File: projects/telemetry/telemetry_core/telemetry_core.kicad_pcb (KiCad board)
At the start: 2 copper layers, 109.3 x 58.3 mm, 60 parts, among them J1 MM_F_RA_20, J2 JST_SM06B-GHS-TB_LF__SN_, J3 CONN_02X03, U1 ATMEGA16M1, U2 TPS560430YF, U3 MCP79511-I_MS, U4 TXB0104PW, U5 LM3480-3.3, U6 MCP2561-E_SN, Y1 Crystal_SMD, Y2 Crystal_32_768kHz

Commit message: feat: begin layout process
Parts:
- moved L1 212.4 mm to (155.2, 43.0), turned to 90 degrees
- moved R11 140.7 mm to (75.1, 120.9)
- moved R5 134.3 mm to (64.9, 89.4)
- moved Y2 132.4 mm to (85.3, 121.3), turned to 90 degrees
- moved U3 130.7 mm to (80.1, 120.5), turned to 180 degrees
- moved R1 127.2 mm to (61.5, 94.4), turned to 90 degrees
- moved C12 126.8 mm to (76.1, 123.1)
- moved C9 123.9 mm to (88.4, 122.3)
- moved C10 121.5 mm to (88.4, 120.3)
- moved D4 121.2 mm to (62.7, 131.6), turned to 180 degrees
- moved D5 120.6 mm to (58.3, 131.6), turned to 180 degrees
- moved D6 120.2 mm to (53.8, 131.6), turned to 180 degrees
- moved R7 118.6 mm to (61.7, 128.9)
- moved TP3 118.5 mm to (53.1, 125.5), turned to 180 degrees
- moved R8 117.5 mm to (57.1, 128.9)
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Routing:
- net GND: track 65.5 -> 105.6 mm, vias 11 -> 27
- net Net-(C2-Pad1): track 0.00 -> 14.8 mm
- net +5V: track 0.00 -> 11.8 mm
- net /12V: track 13.1 -> 19.6 mm
- net +3V3: track 0.00 -> 5.86 mm
- net Net-(C9-Pad1): track 0.00 -> 5.84 mm
- net Net-(C10-Pad1): track 0.00 -> 5.83 mm
- net /P_LED_1: track 0.00 -> 3.06 mm
- net /P_LED_2: track 0.00 -> 2.90 mm
- net /12V_IN: track 0.00 -> 2.66 mm
- net Net-(C7-Pad1): track 0.00 -> 2.61 mm
- net /P_LED_3: track 0.00 -> 2.58 mm
- net /CAN_N: track 0.00 -> 2.49 mm
- net Net-(C5-Pad1): track 0.00 -> 2.41 mm
- net /CAN_P: track 0.00 -> 2.28 mm
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
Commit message: feat: near-complete layout
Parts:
- removed L1: L_100uH, footprints:L_100uH_OEM
- moved C16 150.6 mm to (193.0, 115.3), turned to 270 degrees
- moved U6 140.7 mm to (189.2, 112.3), turned to 90 degrees
- moved R12 139.6 mm to (193.0, 111.8), turned to 90 degrees
- moved C2 138.3 mm to (196.1, 119.6), turned to 90 degrees
- moved R5 137.5 mm to (198.0, 123.8), turned to 270 degrees
- moved C1 134.4 mm to (191.8, 118.2), turned to 180 degrees
- moved R1 134.1 mm to (193.0, 120.4), turned to 0 degrees
- moved U1 127.6 mm to (191.6, 126.9), turned to 270 degrees
- moved C7 120.6 mm to (180.5, 124.2)
- moved Y1 120.6 mm to (182.1, 127.1)
- moved C5 120.6 mm to (184.7, 125.6)
- moved C11 112.9 mm to (184.2, 116.5), turned to 0 degrees
- moved U4 106.4 mm to (182.0, 120.3), turned to 0 degrees
- moved R11 100.2 mm to (175.1, 116.8), turned to 270 degrees
- moved D4 99.8 mm to (162.6, 132.3)
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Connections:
- L101 pad 1: Net-(C103-Pad2) -> Net-(C6-Pad2)
- L101 pad 2: Net-(COUT101-Pad1) -> Net-(COUT1-Pad1)
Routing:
- net +5V: track 11.8 -> 35.5 mm
- net /RXD_RADIO: track 0.00 -> 23.3 mm
- net Net-(COUT101-Pad1): track 17.3 -> 0.00 mm
- net /MOSI: track 0.00 -> 16.5 mm
- net /CAN_RX: track 0.00 -> 15.1 mm
- net /12V: track 19.6 -> 33.7 mm
- net /CSB: track 0.00 -> 9.33 mm
- net /CAN_TX: track 0.00 -> 8.95 mm
- net /SI_ATMEGA: track 0.00 -> 8.49 mm
- net /RTS_RADIO: track 0.00 -> 7.40 mm
- net /CTS_RADIO: track 0.00 -> 7.21 mm
- net Net-(C7-Pad1): track 2.61 -> 9.42 mm
- net Net-(C6-Pad2): track 0.00 -> 5.44 mm
- net Net-(C103-Pad2): track 5.44 -> 0.00 mm
- net /SO_ATMEGA: track 0.00 -> 5.23 mm
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- added copper zone on F.Cu, net +3V3
- added copper zone on F.Cu, net +5V

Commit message: feat: complete v1 layout
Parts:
- moved TP6 128.6 mm to (182.1, 126.0), turned to 270 degrees
- moved TP4 100.7 mm to (169.7, 109.0), turned to 270 degrees
- moved TP5 94.8 mm to (172.6, 102.6), turned to 270 degrees
- moved C14 82.2 mm to (131.7, 114.3)
- moved U5 82.2 mm to (134.6, 114.4)
- moved C13 82.2 mm to (137.8, 114.3)
- moved J3 73.2 mm to (172.2, 146.7), turned to 270 degrees
- moved C15 61.8 mm to (176.0, 94.1), turned to 0 degrees
- moved D7 60.0 mm to (166.6, 97.9)
- moved J1 58.4 mm to (159.4, 90.8), turned to 270 degrees
- moved D2 55.6 mm to (180.9, 102.6), turned to 180 degrees
- moved J2 52.1 mm to (156.5, 148.6), turned to 0 degrees
- moved R2 50.9 mm to (177.2, 102.7), turned to 0 degrees
- moved R3 50.3 mm to (181.6, 116.2), turned to 90 degrees
- moved R4 49.8 mm to (181.6, 120.1), turned to 90 degrees
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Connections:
- U1 pad 23: /P_LED_3 -> /P_LED_2
- U1 pad 24: /P_LED_2 -> /P_LED_3
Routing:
- net +5V: track 35.5 -> 137.0 mm, vias 0 -> 2
- net /MISO: track 0.00 -> 46.5 mm, vias 0 -> 2
- net /CAN_P: track 6.29 -> 36.6 mm
- net +3V3: track 5.86 -> 35.1 mm, vias 0 -> 2
- net /P_LED_2: track 2.90 -> 31.4 mm, vias 0 -> 2
- net /P_LED_1: track 3.06 -> 30.6 mm, vias 0 -> 2
- net /CAN_N: track 4.27 -> 31.1 mm
- net /P_LED_3: track 2.58 -> 27.3 mm, vias 0 -> 2
- net /RESET: track 2.14 -> 26.0 mm, vias 0 -> 2
- net /MOSI: track 16.5 -> 37.9 mm, vias 0 -> 2
- net /RXD_RADIO: track 23.3 -> 41.3 mm, vias 0 -> 2
- net GND: track 101.7 -> 115.2 mm, vias 28 -> 35
- net /RTS_RADIO: track 7.40 -> 17.1 mm
- net /CTS_RADIO: track 7.21 -> 15.7 mm
- net /12V: track 33.7 -> 27.2 mm
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- added copper zone on F.Cu, net Net-(C6-Pad2)
- added copper zone on F.Cu, net Net-(COUT1-Pad1)
- removed copper zone on F.Cu, net Net-(C103-Pad2)
- removed copper zone on F.Cu, net Net-(COUT101-Pad1)
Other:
- board size 109.3 x 58.3 mm -> 76.2 x 63.5 mm
- board text added: "Telemetry Core | V1.0 Melissa Kazazić '24 03/06/2022"

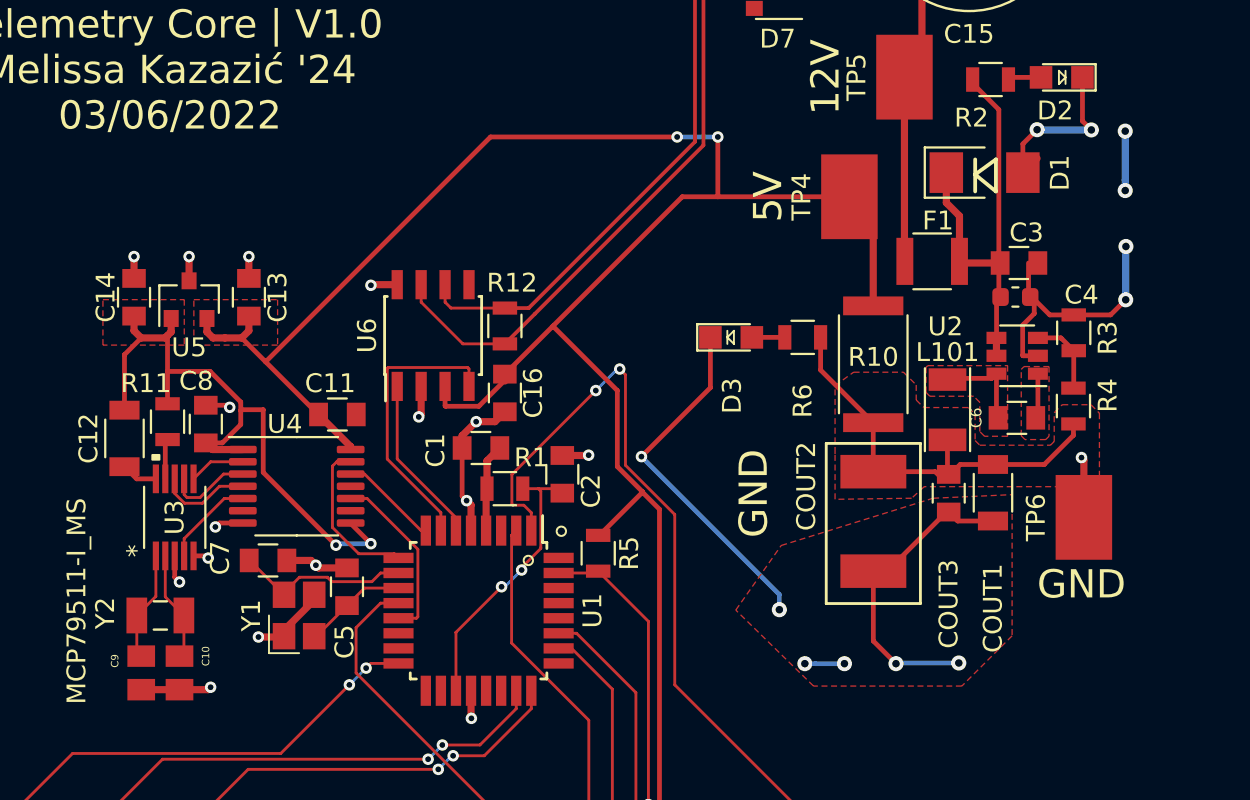
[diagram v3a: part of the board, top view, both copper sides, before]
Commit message: fix: add copper zone
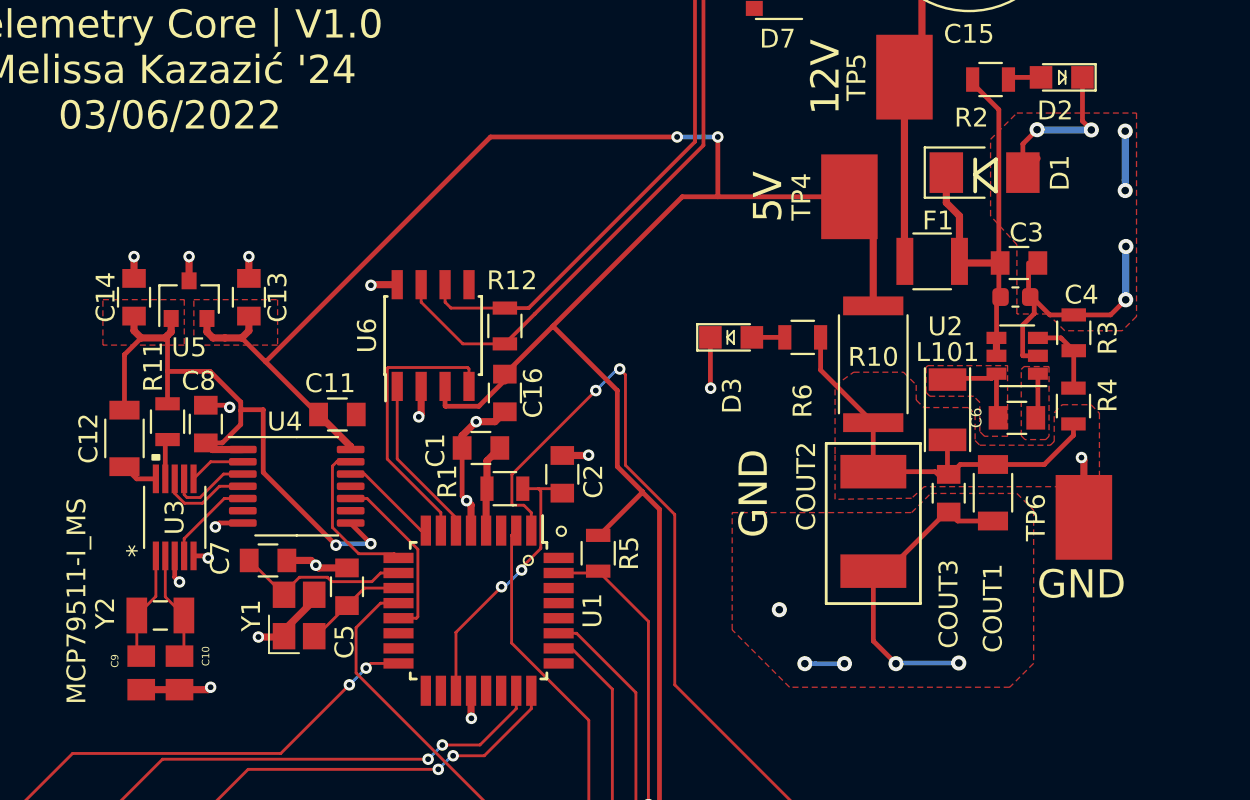
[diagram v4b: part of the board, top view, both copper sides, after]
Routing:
- net GND: track 115.2 -> 98.9 mm
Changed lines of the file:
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@@
     (thickness 1.6)
     (drawings 36)
-    (tracks 467)
+    (tracks 463)
     (zones 0)
     (modules 59)
@@
     (34 B.Paste user)
     (35 F.Paste user)
-    (36 B.SilkS user)
+    (36 B.SilkS user hide)
     (37 F.SilkS user)
     (38 B.Mask user)
@@
     (tags "capacitor 0805")
     (attr smd)
-    (fp_text reference C2 (at -0.889 1.524 90) (layer F.SilkS)
+    (fp_text reference C2 (at -0.381 1.651 90) (layer F.SilkS)
       (effects (font (size 1 1) (thickness 0.15)))
     )
@@
     (tags "capacitor 0805")
     (attr smd)
-    (fp_text reference C8 (at -2.286 0.508) (layer F.SilkS)
+    (fp_text reference C8 (at -2.286 0.381 180) (layer F.SilkS)
       (effects (font (size 1 1) (thickness 0.15)))
     )
@@
       (effects (font (size 1 1) (thickness 0.15)))
     )
-    (fp_line (start 1.75 0.87) (end -1.75 0.87) (layer F.CrtYd) (width 0.05))
-    (fp_line (start 1.75 0.87) (end 1.75 -0.88) (layer F.CrtYd) (width 0.05))
-    (fp_line (start -1.75 -0.88) (end -1.75 0.87) (layer F.CrtYd) (width 0.05))
-    (fp_line (start -1.75 -0.88) (end 1.75 -0.88) (layer F.CrtYd) (width 0.05))
-    (fp_line (start -0.5 0.85) (end 0.5 0.85) (layer F.SilkS) (width 0.12))
-    (fp_line (start 0.5 -0.85) (end -0.5 -0.85) (layer F.SilkS) (width 0.12))
-    (fp_line (start -1 -0.62) (end 1 -0.62) (layer F.Fab) (width 0.1))
-    (fp_line (start 1 -0.62) (end 1 0.62) (layer F.Fab) (width 0.1))
-    (fp_line (start 1 0.62) (end -1 0.62) (layer F.Fab) (width 0.1))
     (fp_line (start -1 0.62) (end -1 -0.62) (layer F.Fab) (width 0.1))
-    (pad 1 smd rect (at -1 0 270) (size 1 1.25) (layers F.Cu F.Paste F.Mask)
-      (net 1 GND))
+    (fp_line (start 1 0.62) (end -1 0.62) (layer F.Fab) (width 0.1))
+    (fp_line (start 1 -0.62) (end 1 0.62) (layer F.Fab) (width 0.1))
+    (fp_line (start -1 -0.62) (end 1 -0.62) (layer F.Fab) (width 0.1))
+    (fp_line (start 0.5 -0.85) (end -0.5 -0.85) (layer F.SilkS) (width 0.12))
+    (fp_line (start -0.5 0.85) (end 0.5 0.85) (layer F.SilkS) (width 0.12))
+    (fp_line (start -1.75 -0.88) (end 1.75 -0.88) (layer F.CrtYd) (width 0.05))
+    (fp_line (start -1.75 -0.88) (end -1.75 0.87) (layer F.CrtYd) (width 0.05))
+    (fp_line (start 1.75 0.87) (end 1.75 -0.88) (layer F.CrtYd) (width 0.05))
+    (fp_line (start 1.75 0.87) (end -1.75 0.87) (layer F.CrtYd) (width 0.05))
     (pad 2 smd rect (at 1 0 270) (size 1 1.25) (layers F.Cu F.Paste F.Mask)
       (net 10 +3V3))
+    (pad 1 smd rect (at -1 0 270) (size 1 1.25) (layers F.Cu F.Paste F.Mask)
+      (net 1 GND))
     (model ${LOCAL_DIR}/OEM_Preferred_Parts/3DModels/C_0805_OEM/C_0805.step
       (at (xyz 0 0 0))
@@
     (tags "resistor 0805")
     (attr smd)
-    (fp_text reference R1 (at 1.397 -1.651 180) (layer F.SilkS)
+    (fp_text reference R1 (at -3.048 -0.381 270) (layer F.SilkS)
       (effects (font (size 1 1) (thickness 0.15)))
     )
@@
     (tags "resistor 0805")
     (attr smd)
-    (fp_text reference R11 (at -2.032 1.143 180) (layer F.SilkS)
+    (fp_text reference R11 (at -2.921 0.762 270) (layer F.SilkS)
       (effects (font (size 1 1) (thickness 0.15)))
     )
@@
     (tags "resistor 0805")
     (attr smd)
-    (fp_text reference R12 (at 2.286 0.381 180) (layer F.SilkS)
+    (fp_text reference R12 (at 2.413 0.381) (layer F.SilkS)
       (effects (font (size 1 1) (thickness 0.15)))
     )
@@
     (tags "TSSOP SO")
     (attr smd)
-    (fp_text reference U4 (at -0.635 -3.302) (layer F.SilkS)
+    (fp_text reference U4 (at -0.635 -3.429) (layer F.SilkS)
       (effects (font (size 1 1) (thickness 0.15)))
     )
@@
   (segment (start 179.63388 106.92892) (end 178.8795 107.6833) (width 0.381) (layer F.Cu) (net 1))
   (via (at 165.95344 130.88366) (size 0.8) (drill 0.4) (layers F.Cu B.Cu) (net 1))
-  (segment (start 165.95344 130.07848) (end 165.95344 130.88366) (width 0.25) (layer B.Cu) (net 1))
-  (segment (start 158.63316 122.7582) (end 158.63316 122.7582) (width 0.25) (layer B.Cu) (net 1))
   (segment (start 178.8795 107.4928) (end 178.8795 107.6833) (width 0.1524) (layer F.Cu) (net 1))
-  (segment (start 162.293 119.09836) (end 158.63316 122.7582) (width 0.254) (layer F.Cu) (net 1))
   (segment (start 162.293 116.429) (end 162.293 119.09836) (width 0.254) (layer F.Cu) (net 1))
   (segment (start 170.942 132.54736) (end 172.14342 133.74878) (width 0.254) (layer F.Cu) (net 1))
@@
   (segment (start 135.635 135.129) (end 135.763 135.001) (width 0.381) (layer F.Cu) (net 1))
   (segment (start 134.112 135.129) (end 135.635 135.129) (width 0.381) (layer F.Cu) (net 1))
-  (segment (start 158.63316 122.7582) (end 165.95344 130.07848) (width 0.25) (layer B.Cu) (net 1))
-  (via (at 158.63316 122.7582) (size 0.6096) (drill 0.3048) (layers F.Cu B.Cu) (net 1))
+  (via (at 162.306 119.126) (size 0.6096) (drill 0.3048) (layers F.Cu B.Cu) (net 1))
   (via (at 136.017 126.492) (size 0.6096) (drill 0.3048) (layers F.Cu B.Cu) (net 1))
   (segment (start 136.226 126.283) (end 136.017 126.492) (width 0.254) (layer F.Cu) (net 1))
@@
   )
   (zone (net 1) (net_name GND) (layer F.Cu) (hatch edge 0.508)
-    (connect_pads yes (clearance 0.1524))
-    (min_thickness 0.1524)
-    (fill yes (arc_segments 16) (thermal_gap 0.508) (thermal_bridge_width 0.508))
+    (connect_pads (clearance 0.1524))
+    (min_thickness 0.254)
+    (fill yes (arc_segments 32) (thermal_gap 0.508) (thermal_bridge_width 0.508))
+    (polygon
+      (pts
+        (xy 184.912 115.316) (xy 184.15 116.078) (xy 181.102 116.078) (xy 180.213 115.189) (xy 178.562 115.189)
+        (xy 178.562 111.506) (xy 177.165 109.982) (xy 177.165 105.918) (xy 178.562 104.521) (xy 184.912 104.521)
+      )
+    )
+  )
+  (zone (net 1) (net_name GND) (layer F.Cu) (hatch edge 0.508)
+    (connect_pads (clearance 0.1524))
+    (min_thickness 0.254)
+    (fill yes (arc_segments 32) (thermal_gap 0.508) (thermal_bridge_width 0.508))
     (polygon
       (pts
-        (xy 178.308 132.2705) (xy 175.641 134.9375) (xy 167.767 134.9375) (xy 163.6395 130.90525) (xy 166.0525 127.47625)
-        (xy 174.117 124.968) (xy 178.308 124.7775)
+        (xy 179.451 125.603) (xy 179.451 133.731) (xy 178.181 135.001) (xy 166.497 135.001) (xy 163.449 131.953)
+        (xy 163.449 125.73) (xy 172.974 125.73) (xy 173.99 124.714) (xy 178.562 124.714)
       )
     )
